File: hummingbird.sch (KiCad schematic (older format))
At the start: 34 parts

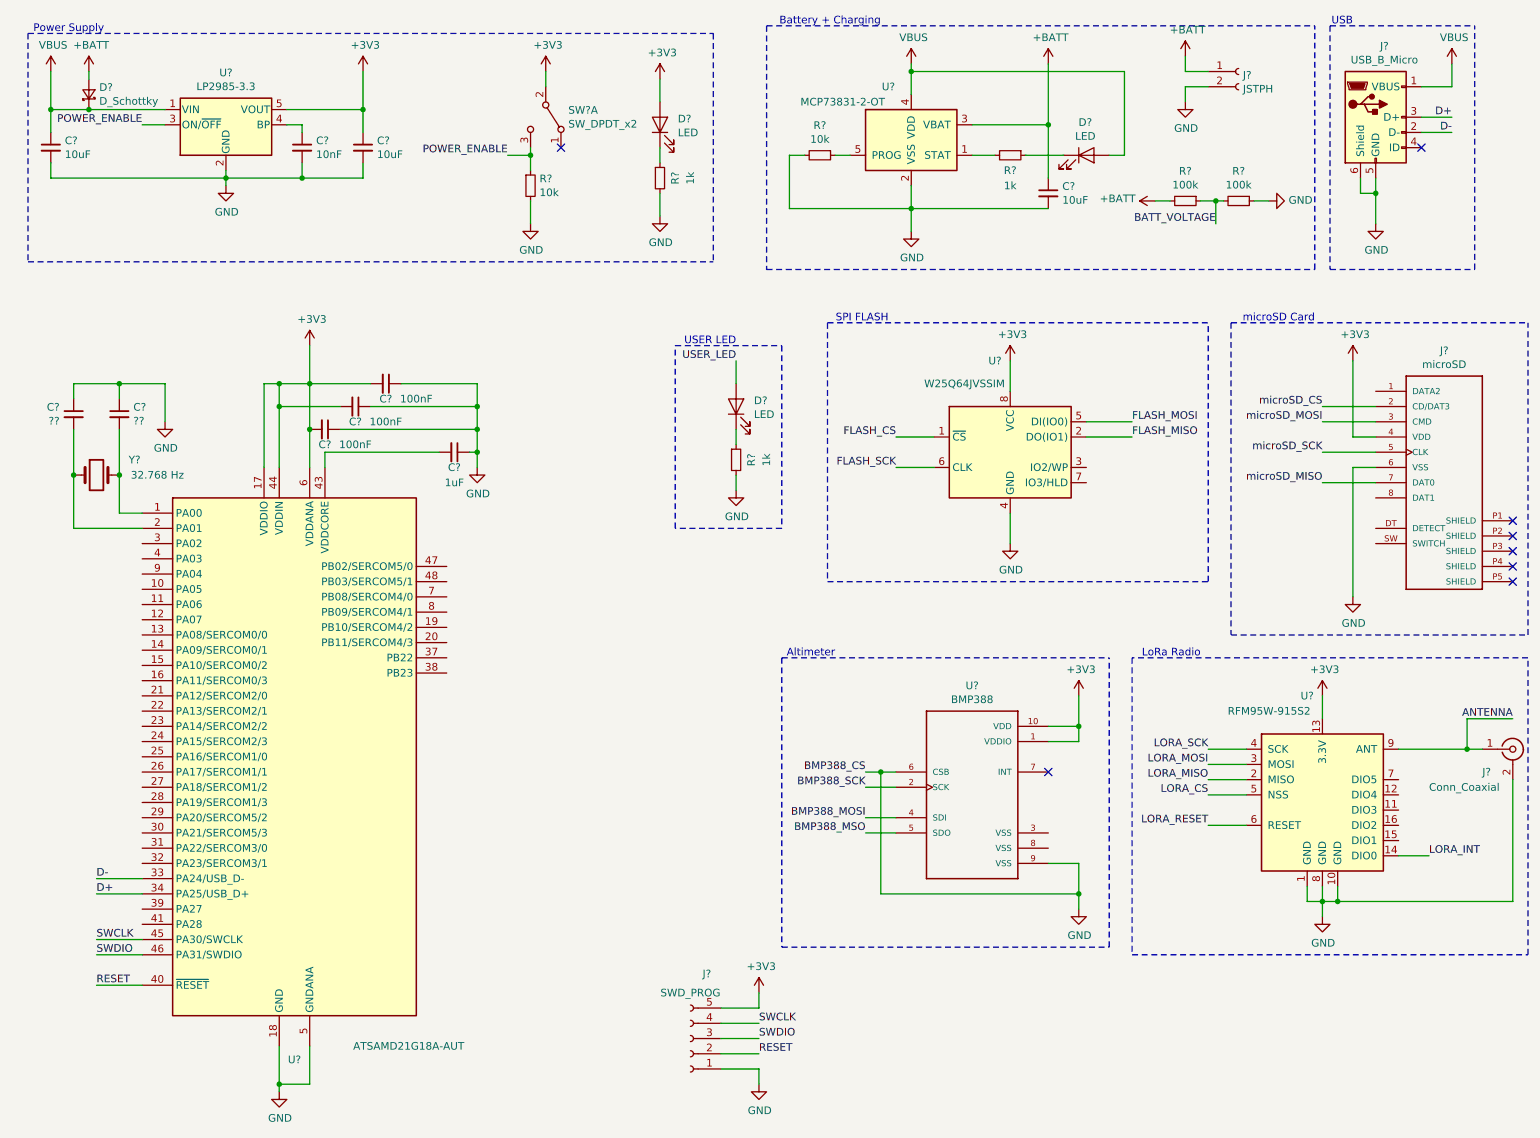
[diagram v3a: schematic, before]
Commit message: add sercom labels, wire up SD card and BMP388
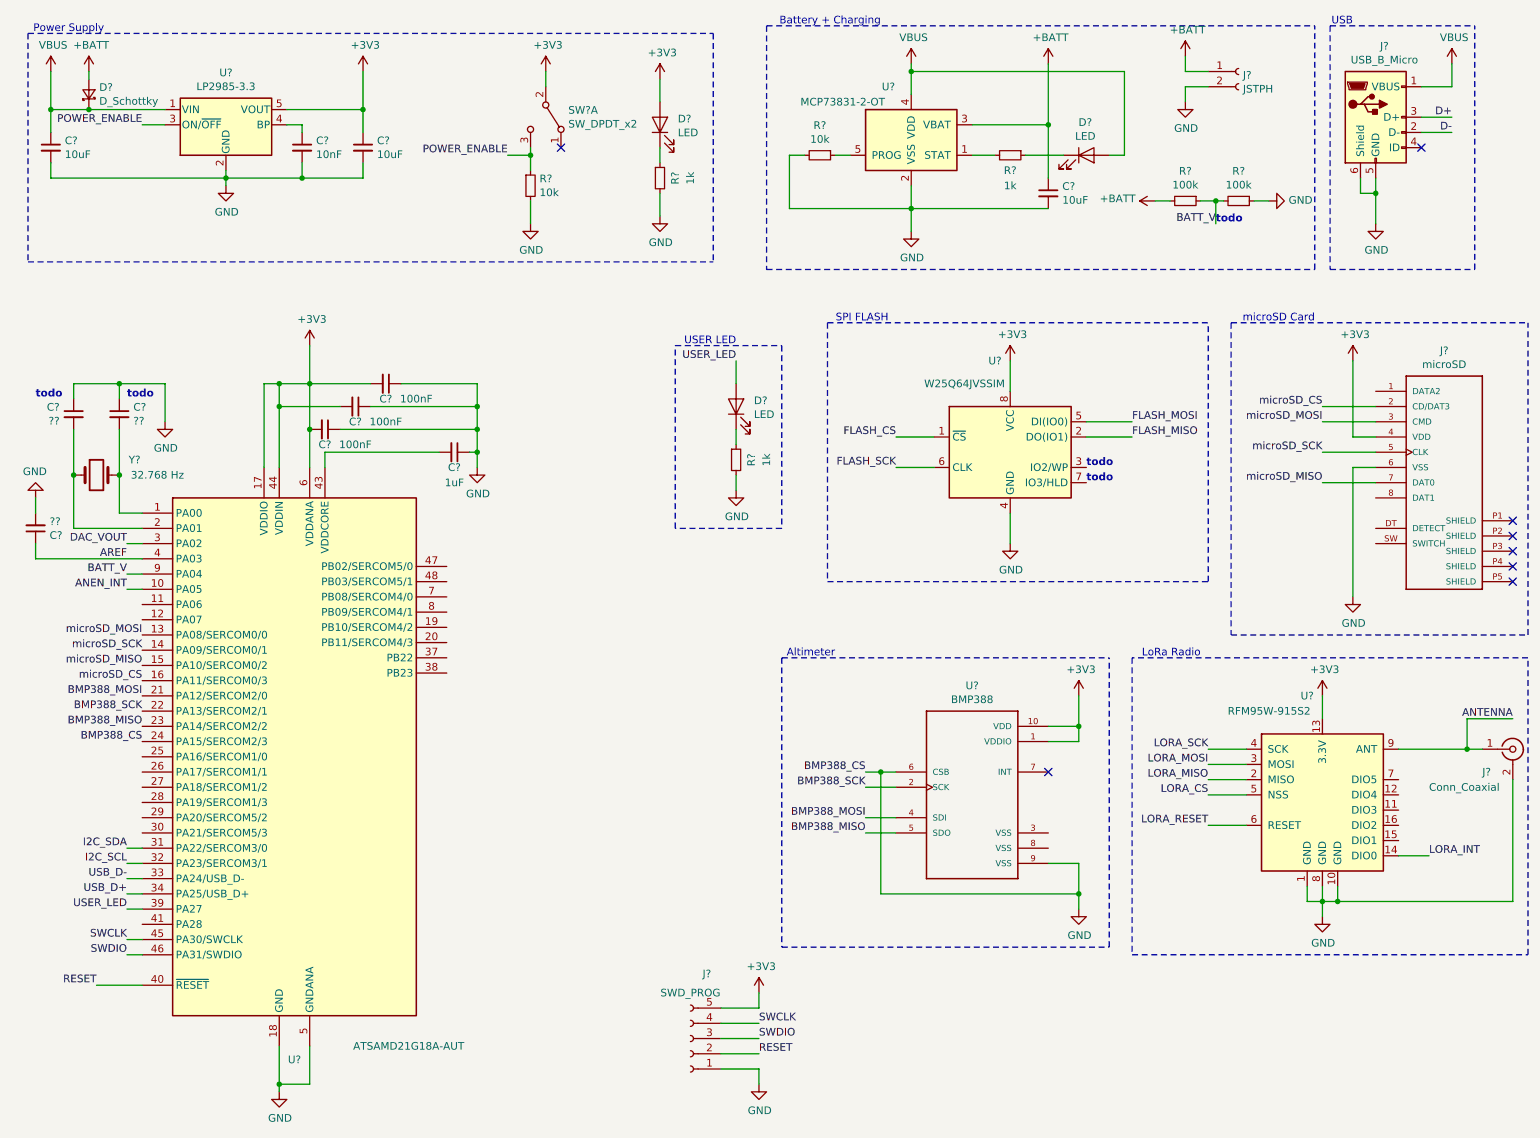
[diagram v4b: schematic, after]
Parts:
- added C?: ??, symbol Device:C_Small
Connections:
- net BATT_VOLTAGE is gone; now on net BATT_V: R?.1, R?.2
- net BMP388_MSO is gone; now on net BMP388_MISO: U?.5 (SDO)
- net BMP388_MOSI: now also U?.21 (PA12/SERCOM2/0)
- net BMP388_SCK: now also U?.22 (PA13/SERCOM2/1)
- net D+: no longer U?.34 (PA25/USB_D+)
- net D-: no longer U?.33 (PA24/USB_D-)
- net GND: now also U?.24 (PA15/SERCOM2/3), C?.2
- net USER_LED: now also U?.39 (PA27)
- net microSD_CS: now also U?.16 (PA11/SERCOM0/3)
- net microSD_MISO: now also U?.15 (PA10/SERCOM0/2)
- net microSD_MOSI: now also U?.13 (PA08/SERCOM0/0)
- net microSD_SCK: now also U?.14 (PA09/SERCOM0/1)
- net ANEN_INT: now reaches U?.10 (PA05)
- net BMP388_MISO: now reaches U?.23 (PA14/SERCOM2/2)
- net DAC_VOUT: now reaches U?.3 (PA02)
- net I2C_SDA: now reaches U?.31 (PA22/SERCOM3/0)
- net I2C_SCL: now reaches U?.32 (PA23/SERCOM3/1)
- net AREF: now reaches U?.4 (PA03)
- net AREF: now also C?.1
- net BATT_V: now reaches U?.9 (PA04)
- new net USB_D+: U?.34 (PA25/USB_D+)
- new net USB_D-: U?.33 (PA24/USB_D-)
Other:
- note added: "todo"
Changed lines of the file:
@@
 	1    0    0    -1
 $EndComp
-Text Label 1050 6700 0    50   ~ 0
+Text Label 1250 6700 2    50   ~ 0
 SWDIO
-Text Label 1050 6600 0    50   ~ 0
+Text Label 1250 6600 2    50   ~ 0
 SWCLK
-Wire Wire Line
-	1350 6700 1050 6700
-Wire Wire Line
-	1350 6600 1050 6600
-Text Label 1050 6900 0    50   ~ 0
+Text Label 1050 6900 2    50   ~ 0
 RESET
 Wire Wire Line
@@
 D-
 NoConn ~ 9750 1400
-Wire Wire Line
-	1350 6300 1050 6300
-Text Label 1050 6300 0    50   ~ 0
-D+
-Wire Wire Line
-	1350 6200 1050 6200
-Text Label 1050 6200 0    50   ~ 0
-D-
+Text Label 1250 6300 2    50   ~ 0
+USB_D+
+Text Label 1250 6200 2    50   ~ 0
+USB_D-
 $Comp
 L Switch:SW_DPDT_x2 SW?
@@
 	8400 1750 8450 1750
 Text Label 8400 1900 2    50   ~ 0
-BATT_VOLTAGE
+BATT_V
 Text Notes 5900 4750 2    50   ~ 0
 Altimeter
@@
 	6300 5900 6100 5900
 Text Label 6100 5900 2    50   ~ 0
-BMP388_MSO
+BMP388_MISO
 NoConn ~ 7300 5500
 $Comp
@@
 Text Label 5400 7350 0    50   ~ 0
 RESET
+Text Notes 7550 3500 0    50   ~ 10
+todo
+Text Notes 7550 3600 0    50   ~ 10
+todo
+Text Notes 8400 1900 0    50   ~ 10
+todo
+Text Notes 650  3050 0    50   ~ 10
+todo
+Text Notes 1250 3050 0    50   ~ 10
+todo
+Text Label 1250 6400 2    50   ~ 0
+USER_LED
+Text Label 1250 4200 2    50   ~ 0
+BATT_V
+Wire Wire Line
+	1350 4100 650  4100
+$Comp
+L Device:C_Small C?
+U 1 1 5CFEE4CF
+P 650 3900
+F 0 "C?" H 742 3946 50  0000 L CNN
+F 1 "??" H 742 3855 50  0000 L CNN
+F 2 "" H 650 3900 50  0001 C CNN
+F 3 "~" H 650 3900 50  0001 C CNN
+	1    650  3900
+	1    0    0    1
+$EndComp
+$Comp
+L power:GND #PWR?
+U 1 1 5CFEE83D
+P 650 3700
+F 0 "#PWR?" H 650 3450 50  0001 C CNN
+F 1 "GND" H 655 3527 50  0000 C CNN
+F 2 "" H 650 3700 50  0001 C CNN
+F 3 "" H 650 3700 50  0001 C CNN
+	1    650  3700
+	-1   0    0    1
+$EndComp
+Wire Wire Line
+	650  3800 650  3700
+Text Label 1250 4100 2    50   ~ 0
+AREF
+Text Label 1250 4000 2    50   ~ 0
+DAC_VOUT
+Text Label 1250 4300 2    50   ~ 0
+ANEN_INT
+Wire Wire Line
+	1350 4000 1250 4000
+Wire Wire Line
+	1250 4200 1350 4200
+Wire Wire Line
+	1250 4300 1350 4300
+Wire Wire Line
+	650  4000 650  4100
+Wire Wire Line
+	1350 6000 1250 6000
+Text Label 1250 6000 2    50   ~ 0
+I2C_SDA
+Wire Wire Line
+	1350 6100 1250 6100
+Text Label 1250 6100 2    50   ~ 0
+I2C_SCL
+Wire Wire Line
+	1250 6200 1350 6200
+Wire Wire Line
+	1350 6300 1250 6300
+Wire Wire Line
+	1250 6400 1350 6400
+Wire Wire Line
+	1250 6600 1350 6600
+Wire Wire Line
+	1250 6700 1350 6700
+Text Label 1350 4900 2    50   ~ 0
+microSD_CS
+Text Label 1350 4600 2    50   ~ 0
+microSD_MOSI
+Text Label 1350 4700 2    50   ~ 0
+microSD_SCK
+Text Label 1350 4800 2    50   ~ 0
+microSD_MISO
+Text Label 1350 5300 2    50   ~ 0
+BMP388_CS
+Text Label 1350 5100 2    50   ~ 0
+BMP388_SCK
+Text Label 1350 5000 2    50   ~ 0
+BMP388_MOSI
+Text Label 1350 5200 2    50   ~ 0
+BMP388_MISO
 $EndSCHEMATC

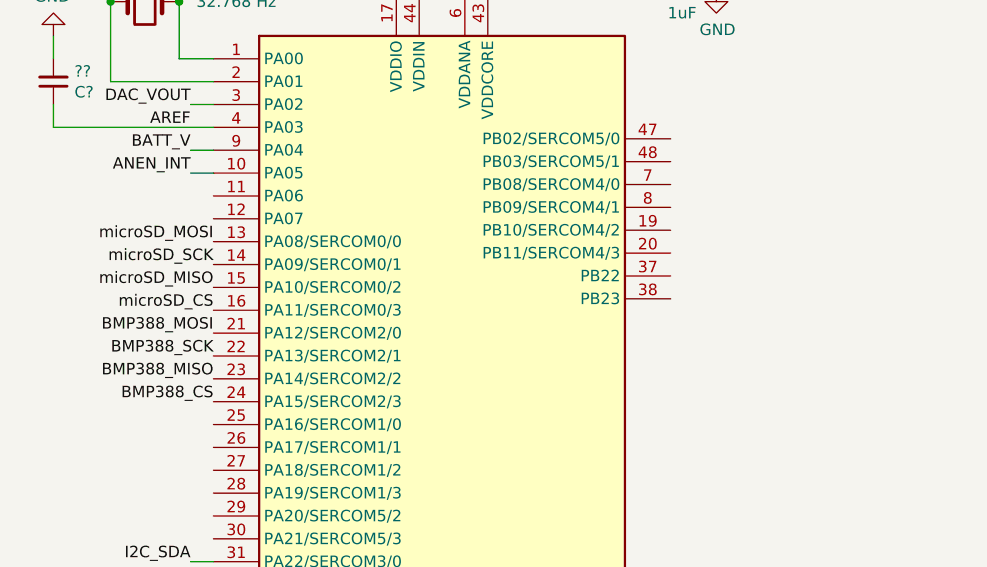
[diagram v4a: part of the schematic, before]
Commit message: Add LoRa Spi connections
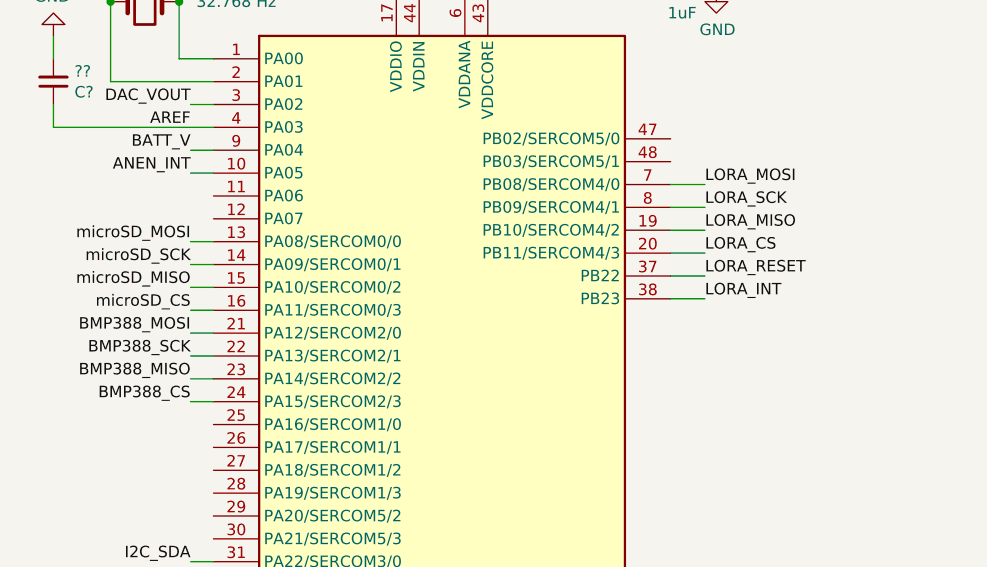
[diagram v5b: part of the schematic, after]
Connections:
- net LORA_CS: now also U?.20 (PB11/SERCOM4/3)
- net LORA_INT: now also U?.38 (PB23)
- net LORA_MISO: now also U?.19 (PB10/SERCOM4/2)
- net LORA_MOSI: now also U?.7 (PB08/SERCOM4/0)
- net LORA_RESET: now also U?.37 (PB22)
- net LORA_SCK: now also U?.8 (PB09/SERCOM4/1)
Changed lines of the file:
@@
 Wire Wire Line
 	1250 6700 1350 6700
-Text Label 1350 4900 2    50   ~ 0
+Text Label 1250 4900 2    50   ~ 0
 microSD_CS
-Text Label 1350 4600 2    50   ~ 0
+Text Label 1250 4600 2    50   ~ 0
 microSD_MOSI
-Text Label 1350 4700 2    50   ~ 0
+Text Label 1250 4700 2    50   ~ 0
 microSD_SCK
-Text Label 1350 4800 2    50   ~ 0
+Text Label 1250 4800 2    50   ~ 0
 microSD_MISO
-Text Label 1350 5300 2    50   ~ 0
+Text Label 1250 5300 2    50   ~ 0
 BMP388_CS
-Text Label 1350 5100 2    50   ~ 0
+Text Label 1250 5100 2    50   ~ 0
 BMP388_SCK
-Text Label 1350 5000 2    50   ~ 0
+Text Label 1250 5000 2    50   ~ 0
 BMP388_MOSI
-Text Label 1350 5200 2    50   ~ 0
+Text Label 1250 5200 2    50   ~ 0
 BMP388_MISO
+Text Label 3500 4450 0    50   ~ 0
+LORA_SCK
+Wire Wire Line
+	1250 4600 1350 4600
+Wire Wire Line
+	1250 4700 1350 4700
+Wire Wire Line
+	1250 4800 1350 4800
+Wire Wire Line
+	1250 4900 1350 4900
+Wire Wire Line
+	1250 5000 1350 5000
+Wire Wire Line
+	1250 5100 1350 5100
+Wire Wire Line
+	1250 5200 1350 5200
+Wire Wire Line
+	1250 5300 1350 5300
+Wire Wire Line
+	3350 4450 3500 4450
+Text Label 3500 4350 0    50   ~ 0
+LORA_MOSI
+Text Label 3500 4550 0    50   ~ 0
+LORA_MISO
+Text Label 3500 4650 0    50   ~ 0
+LORA_CS
+Text Label 3500 4750 0    50   ~ 0
+LORA_RESET
+Text Label 3500 4850 0    50   ~ 0
+LORA_INT
+Wire Wire Line
+	3350 4350 3500 4350
+Wire Wire Line
+	3350 4550 3500 4550
+Wire Wire Line
+	3350 4650 3500 4650
+Wire Wire Line
+	3350 4750 3500 4750
+Wire Wire Line
+	3350 4850 3500 4850
 $EndSCHEMATC
